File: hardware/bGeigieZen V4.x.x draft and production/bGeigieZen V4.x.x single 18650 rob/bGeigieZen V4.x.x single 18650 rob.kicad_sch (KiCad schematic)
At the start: 10 parts, among them J1 M5 2x15 pin, J2 Geiger IRover, J3 GPS, J4 Geiger Safepulse, J5 Extra support header

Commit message: Update V4.0.5 boards.
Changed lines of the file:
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@@
 	(title_block
 		(title "bGeigieZen V4.0.5 rNFW")
-		(date "2024-05-23")
+		(date "2024-05-31")
 		(rev "V4.0.5 NFW")
 		(company "GitHub link at https://github.com/Safecast/bGeigieZen")
@@
 		)
 		(property "Value" "Crowbar"
-			(at 99.06 88.9 90)
-			(effects
-				(font
+			(at 97.9131 90.1956 90)
+			(effects
+				(font

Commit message: added fuse to the 4.0.5 NFW board. Just to be safe:)
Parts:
- added F1: Fuse_Small, Fuse:Fuse_Littelfuse_395Series, symbol Device:Fuse_Small
- BT1: value 3.7 V Lipo -> 3.7 V Lipo
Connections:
- net BAT: now also F1.2; no longer BT1.1 (+)
- new net: BT1.1 (+), F1.1
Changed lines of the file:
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@@
-	)
-	(junction
-		(at 93.98 76.2)
-		(diameter 0)
-		(color 0 0 0 0)
 	)
 	(junction
@@
 	)
 	(junction
+		(at 107.95 76.2)
+		(diameter 0)
+		(color 0 0 0 0)
+	)
+	(junction
 		(at 130.81 78.74)
 		(diameter 0.3048)
@@
 	(wire
 		(pts
+			(xy 107.95 76.2) (xy 107.95 82.55)
+		)
+		(stroke
+			(width 0)
+			(type default)
+		)
+	)
+	(wire
+		(pts
 			(xy 127 120.65) (xy 127 96.52)
 		)
@@
 	(wire
 		(pts
+			(xy 100.33 76.2) (xy 107.95 76.2)
+		)
+		(stroke
+			(width 0)
+			(type default)
+		)
+	)
+	(wire
+		(pts
 			(xy 107.95 64.77) (xy 107.95 73.66)
 		)
@@
 	(wire
 		(pts
-			(xy 107.95 73.66) (xy 107.95 82.55)
+			(xy 107.95 73.66) (xy 107.95 76.2)
 		)
 		(stroke
@@
 	(wire
 		(pts
-			(xy 93.98 73.66) (xy 93.98 76.2)
-		)
-		(stroke
-			(width 0)
-			(type default)
-		)
-	)
-	(wire
-		(pts
-			(xy 93.98 76.2) (xy 93.98 78.74)
-		)
-		(stroke
-			(width 0)
-			(type default)
-		)
-	)
-	(wire
-		(pts
-			(xy 93.98 73.66) (xy 107.95 73.66)
+			(xy 93.98 73.66) (xy 93.98 78.74)
+		)
+		(stroke
+			(width 0)
+			(type default)
+		)
+	)
+	(wire
+		(pts
+			(xy 93.98 73.66) (xy 99.06 73.66)
 		)
 		(stroke
@@
 	(wire
 		(pts
+			(xy 104.14 73.66) (xy 107.95 73.66)
+		)
+		(stroke
+			(width 0)
+			(type default)
+		)
+	)
+	(wire
+		(pts
 			(xy 166.37 74.93) (xy 184.15 74.93)
 		)
@@
 		(pts
 			(xy 151.765 64.77) (xy 151.765 111.76)
-		)
-		(stroke
-			(width 0)
-			(type default)
-		)
-	)
-	(wire
-		(pts
-			(xy 100.33 76.2) (xy 93.98 76.2)
 		)
 		(stroke
@@
 			)
 		)
-		(property "Value" " 3.7 V Lipo"
+		(property "Value" "3.7 V Lipo"
 			(at 80.5275 87.2043 0)
 			(effects
@@
 					(unit 1)
 				)
+			)
+		)
+	)
+	(symbol
+		(lib_id "Device:Fuse_Small")
+		(at 101.6 73.66 0)
+		(unit 1)
+		(exclude_from_sim no)
+		(in_bom yes)
+		(on_board yes)
+		(dnp no)
+		(fields_autoplaced yes)
+		(property "Reference" "F1"
+			(at 101.6 68.58 0)
+			(effects
+				(font
+					(size 1.27 1.27)
+				)
+			)
+		)
+		(property "Value" "Fuse_Small"
+			(at 101.6 71.12 0)
+			(effects
+				(font
+					(size 1.27 1.27)
+				)
+			)
+		)
+		(property "Footprint" "Fuse:Fuse_Littelfuse_395Series"
+			(at 101.6 73.66 0)
+			(effects
+				(font
+					(size 1.27 1.27)
+				)
+				(hide yes)
+			)
+		)
+		(property "Datasheet" "~"
+			(at 101.6 73.66 0)
+			(effects
+				(font
+					(size 1.27 1.27)
+				)
+				(hide yes)
+			)
+		)
+		(property "Description" "Fuse, small symbol"
+			(at 101.6 73.66 0)
+			(effects
+				(font
+					(size 1.27 1.27)
+				)
+				(hide yes)
+			)
+		)
+		(pin "2"
+		)
+		(pin "1"
+		)
+		(instances
+			(project ""
+				(path "/c2e3a215-6a49-419d-95d1-595f35b17280"
+					(reference "F1")
+					(unit 1)
+				)

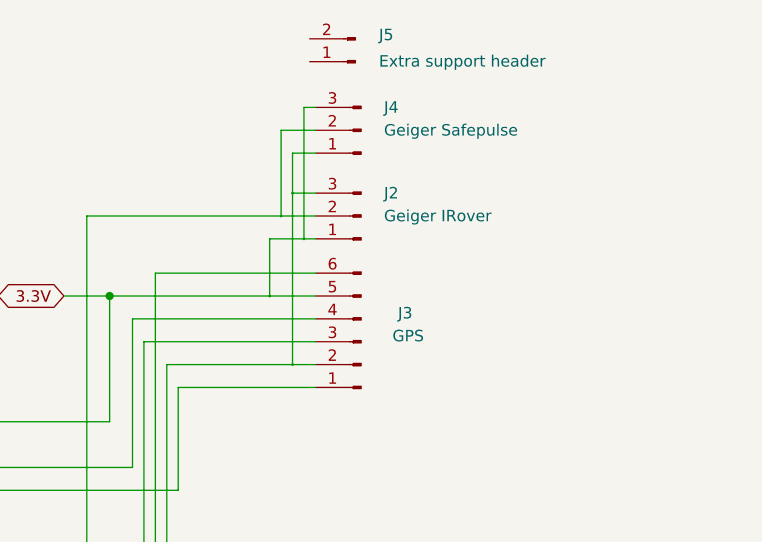
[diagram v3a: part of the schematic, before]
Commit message: Mini  fuse added and 3d files for 4.0.5 NFW
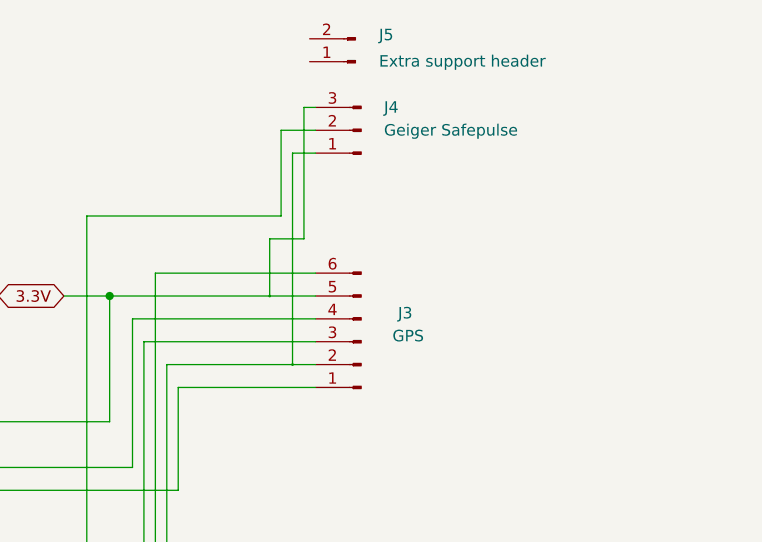
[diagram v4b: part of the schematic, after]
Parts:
- removed J2: Geiger IRover, Connector_PinHeader_2.54mm:PinHeader_1x03_P2.54mm_Vertical, symbol Connector:Conn_01x03_Male
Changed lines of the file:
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@@
 	(title_block
 		(title "bGeigieZen V4.0.5 rNFW")
-		(date "2024-06-07")
+		(date "2024-06-17")
 		(rev "V4.0.5 NFW")
 		(company "GitHub link at https://github.com/Safecast/bGeigieZen")
@@
 	)
 	(junction
-		(at 186.69 63.5)
-		(diameter 0.3048)
-		(color 0 0 0 0)
-	)
-	(junction
-		(at 185.42 66.04)
-		(diameter 0.3048)
-		(color 0 0 0 0)
-	)
-	(junction
 		(at 184.15 74.93)
-		(diameter 0.3048)
-		(color 0 0 0 0)
-	)
-	(junction
-		(at 187.96 68.58)
 		(diameter 0.3048)
 		(color 0 0 0 0)
@@
 	(wire
 		(pts
-			(xy 189.23 66.04) (xy 185.42 66.04)
-		)
-		(stroke
-			(width 0)
-			(type solid)
-		)
-	)
-	(wire
-		(pts
 			(xy 93.98 86.36) (xy 93.98 88.9)
 		)
@@
 	(wire
 		(pts
-			(xy 186.69 82.55) (xy 186.69 63.5)
+			(xy 186.69 59.055) (xy 186.69 82.55)
 		)
 		(stroke
@@
 	(wire
 		(pts
-			(xy 187.96 68.58) (xy 189.23 68.58)
-		)
-		(stroke
-			(width 0)
-			(type solid)
-		)
-	)
-	(wire
-		(pts
 			(xy 129.54 99.06) (xy 133.35 99.06)
 		)
@@
 	(wire
 		(pts
-			(xy 186.69 63.5) (xy 186.69 59.055)
-		)
-		(stroke
-			(width 0)
-			(type solid)
-		)
-	)
-	(wire
-		(pts
 			(xy 151.765 64.77) (xy 151.765 111.76)
 		)
@@
 			(width 0)
 			(type default)
-		)
-	)
-	(wire
-		(pts
-			(xy 186.69 63.5) (xy 189.23 63.5)
-		)
-		(stroke
-			(width 0)
-			(type solid)
 		)
 	)
@@
 					(unit 1)
 				)
-			)
-		)
-	)
-	(symbol
-		(lib_id "Connector:Conn_01x03_Male")
-		(at 194.31 66.04 180)
-		(unit 1)
-		(exclude_from_sim no)
-		(in_bom yes)
-		(on_board yes)
-		(dnp no)
-		(property "Reference" "J2"
-			(at 196.85 63.5 0)
-			(effects
-				(font
-					(size 1.27 1.27)
-				)
-				(justify right)
-			)
-		)
-		(property "Value" "Geiger IRover"
-			(at 196.85 66.04 0)
-			(effects
-				(font
-					(size 1.27 1.27)
-				)
-				(justify right)
-			)
-		)
-		(property "Footprint" "Connector_PinHeader_2.54mm:PinHeader_1x03_P2.54mm_Vertical"
-			(at 194.31 66.04 0)
-			(effects
-				(font
-					(size 1.27 1.27)
-				)
-				(hide yes)
-			)
-		)
-		(property "Datasheet" "~"
-			(at 194.31 66.04 0)
-			(effects
-				(font
-					(size 1.27 1.27)
-				)
-				(hide yes)
-			)
-		)
-		(property "Description" ""
-			(at 194.31 66.04 0)
-			(effects
-				(font
-					(size 1.27 1.27)
-				)
-				(hide yes)
-			)
-		)
-		(pin "1"
-		)
-		(pin "2"
-		)
-		(pin "3"
-		)
-		(instances
-			(project "bGeigieZen V4.x.x draft"
-				(path "/c2e3a215-6a49-419d-95d1-595f35b17280"
-					(reference "J2")
-					(unit 1)
-				)

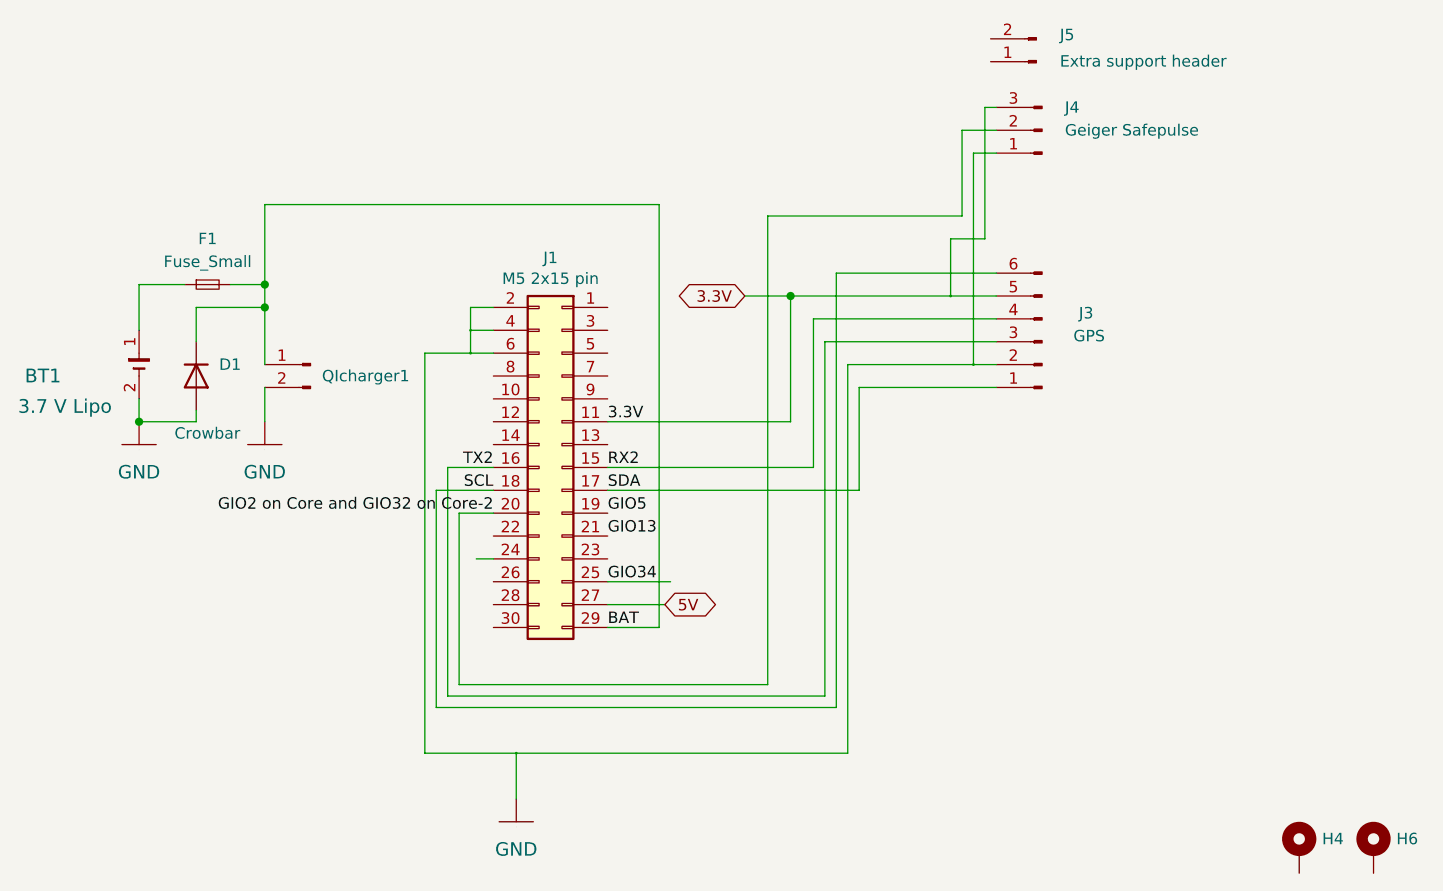
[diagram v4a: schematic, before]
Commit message: Updated boards for Zen V4.0.7
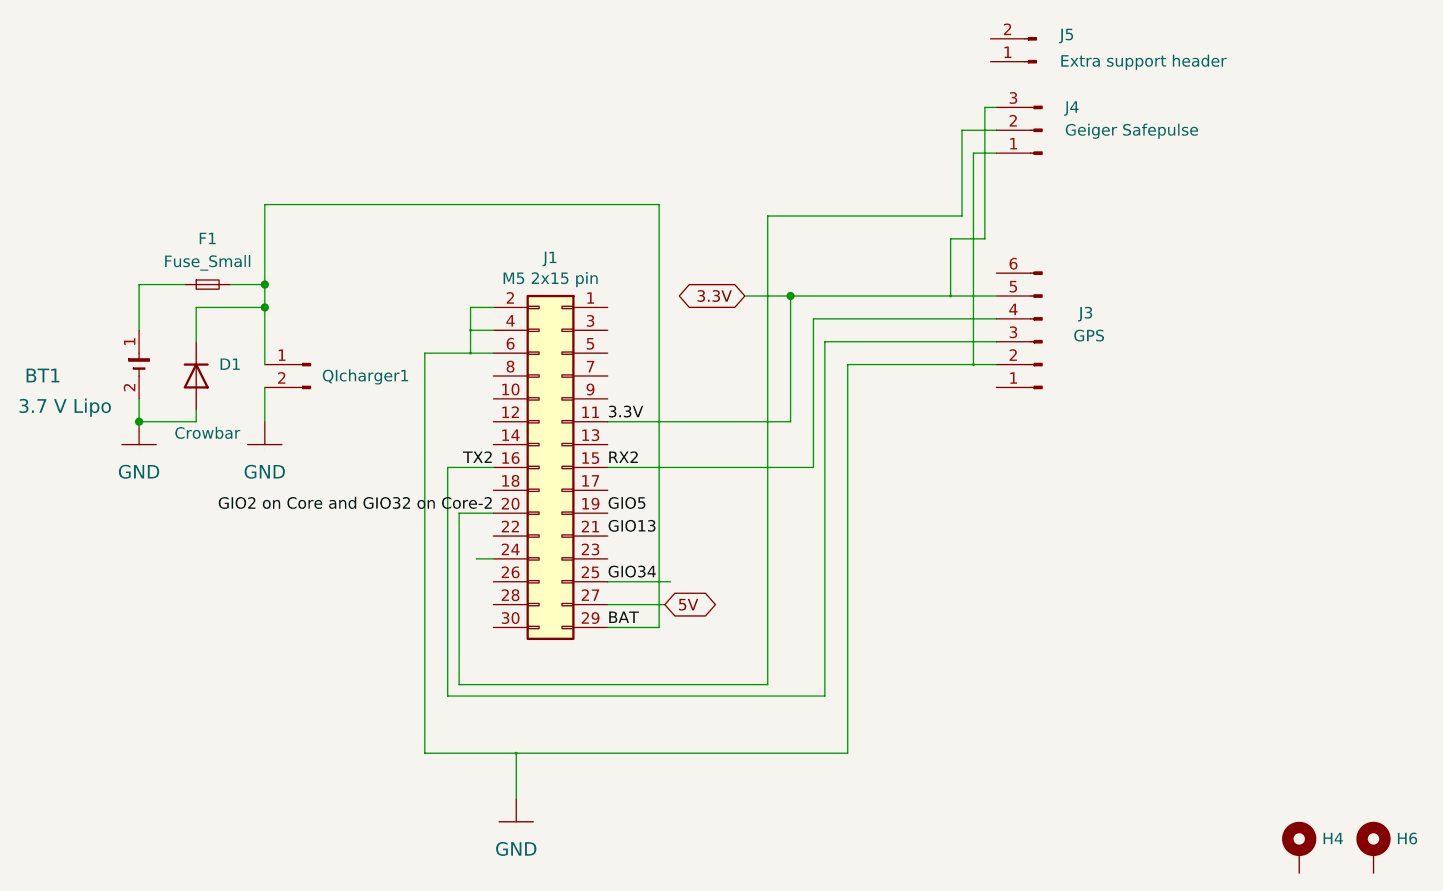
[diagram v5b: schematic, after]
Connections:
- net SCL: no longer names the net of J1.18 (Pin_18)
- net SCL: no longer J3.6 (Pin_6)
- net SDA: no longer names the net of J1.17 (Pin_17)
- net SDA: no longer J3.1 (Pin_1)
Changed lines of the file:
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@@
-	(wire
-		(pts
-			(xy 173.99 85.09) (xy 173.99 96.52)
-		)
-		(stroke
-			(width 0)
-			(type default)
-		)
-	)
-	(wire
-		(pts
-			(xy 127 96.52) (xy 133.35 96.52)
-		)
-		(stroke
-			(width 0)
-			(type default)
-		)
-	)
 	(wire
 		(pts
@@
 	(wire
 		(pts
-			(xy 127 120.65) (xy 127 96.52)
-		)
-		(stroke
-			(width 0)
-			(type default)
-		)
-	)
-	(wire
-		(pts
 			(xy 186.69 59.055) (xy 189.23 59.055)
 		)
@@
 	(wire
 		(pts
-			(xy 189.23 85.09) (xy 173.99 85.09)
-		)
-		(stroke
-			(width 0)
-			(type default)
-		)
-	)
-	(wire
-		(pts
 			(xy 100.33 87.63) (xy 100.33 88.9)
 		)
@@
 	(wire
 		(pts
-			(xy 146.05 96.52) (xy 173.99 96.52)
-		)
-		(stroke
-			(width 0)
-			(type default)
-		)
-	)
-	(wire
-		(pts
 			(xy 130.81 78.74) (xy 130.81 76.2)
 		)
@@
 	(wire
 		(pts
-			(xy 171.45 72.39) (xy 189.23 72.39)
-		)
-		(stroke
-			(width 0)
-			(type default)
-		)
-	)
-	(wire
-		(pts
 			(xy 170.18 80.01) (xy 170.18 119.38)
 		)
@@
 	(wire
 		(pts
-			(xy 171.45 72.39) (xy 171.45 120.65)
-		)
-		(stroke
-			(width 0)
-			(type default)
-		)
-	)
-	(wire
-		(pts
 			(xy 93.98 73.66) (xy 93.98 78.74)
 		)
@@
 			(width 0)
 			(type default)
-		)
-	)
-	(wire
-		(pts
-			(xy 171.45 120.65) (xy 127 120.65)
-		)
-		(stroke
-			(width 0)
-			(type default)
-		)
-	)
-	(label "SDA"
-		(at 146.05 96.52 0)
-		(fields_autoplaced yes)
-		(effects
-			(font
-				(size 1.27 1.27)
-			)
-			(justify left bottom)
 		)
 	)
@@
 		)
 	)
-	(label "SCL"
-		(at 133.35 96.52 180)
-		(fields_autoplaced yes)
-		(effects
-			(font
-				(size 1.27 1.27)
-			)
-			(justify right bottom)
-		)
-	)

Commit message: Added 3d update 3dModel of tube grid and update boards
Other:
- title: bGeigieZen V4.0.5 rNFW -> bGeigieZen V4.0.7rNFW
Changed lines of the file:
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@@
 (kicad_sch
-	(version 20240602)
+	(version 20240620)
 	(generator "eeschema")
 	(generator_version "8.99")
 	(paper "A4")
 	(title_block
-		(title "bGeigieZen V4.0.5 rNFW")
-		(date "2024-06-17")
-		(rev "V4.0.5 NFW")
+		(title "bGeigieZen V4.0.7rNFW")
+		(date "2024-07-27")
+		(rev "V4.0.7 NFW")
 		(company "GitHub link at https://github.com/Safecast/bGeigieZen")
 		(comment 1 "Not For Whimps version")
@@
 		)
 	)
+	(embedded_fonts no)
 )

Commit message: Some more small fixes on the V4.x.x NFW board
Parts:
- renumbered QIcharger1 to QI-charger
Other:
- moved on the sheet: D1
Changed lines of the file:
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@@
 (kicad_sch
-	(version 20240620)
+	(version 20240716)
 	(generator "eeschema")
 	(generator_version "8.99")
@@
 	(wire
 		(pts
-			(xy 100.33 87.63) (xy 100.33 88.9)
+			(xy 100.33 86.36) (xy 100.33 88.9)
 		)
 		(stroke
@@
 	(wire
 		(pts
-			(xy 100.33 80.01) (xy 100.33 76.2)
+			(xy 100.33 78.74) (xy 100.33 76.2)
 		)
 		(stroke
@@
 		(on_board yes)
 		(dnp no)
-		(property "Reference" "QIcharger1"
+		(property "Reference" "QI-charger"
 			(at 114.3 83.82 0)
 			(effects
@@
 			(project "bGeigieZen V4.x.x single 18650"
 				(path "/c2e3a215-6a49-419d-95d1-595f35b17280"
-					(reference "QIcharger1")
+					(reference "QI-charger")
 					(unit 1)
 				)
@@
 	(symbol
 		(lib_id "Device:D")
-		(at 100.33 83.82 270)
+		(at 100.33 82.55 270)
 		(unit 1)
 		(exclude_from_sim no)
@@
 		(dnp no)
 		(property "Reference" "D1"
-			(at 102.87 82.5499 90)
+			(at 102.87 81.2799 90)
 			(effects
 				(font
@@
 		)
 		(property "Value" "Crowbar"
-			(at 97.9131 90.1956 90)
+			(at 97.9131 88.9256 90)
 			(effects
 				(font
@@
 		)
 		(property "Footprint" "Diode_THT:D_DO-201_P15.24mm_Horizontal"
-			(at 100.33 83.82 0)
+			(at 100.33 82.55 0)
 			(effects
 				(font
@@
 		)
 		(property "Datasheet" "~"
-			(at 100.33 83.82 0)
+			(at 100.33 82.55 0)
 			(effects
 				(font
@@
 		)
 		(property "Description" "Diode"
-			(at 100.33 83.82 0)
+			(at 100.33 82.55 0)
 			(effects
 				(font
@@
 		)
 		(property "Sim.Device" "D"
-			(at 100.33 83.82 0)
+			(at 100.33 82.55 0)
 			(effects
 				(font
@@
 		)
 		(property "Sim.Pins" "1=K 2=A"
-			(at 100.33 83.82 0)
-			(effects
-				(font
+			(at 100.33 82.55 0)
+			(effects
+				(font

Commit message: Updated data and layout boards and schematics
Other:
- title: bGeigieZen V4.0.7rNFW -> bGeigieZen V4.0.7 NFW
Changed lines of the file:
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@@
 	(paper "A4")
 	(title_block
-		(title "bGeigieZen V4.0.7rNFW")
-		(date "2024-07-27")
+		(title "bGeigieZen V4.0.7 NFW")
+		(date "2024-08-14")
 		(rev "V4.0.7 NFW")
 		(company "GitHub link at https://github.com/Safecast/bGeigieZen")
